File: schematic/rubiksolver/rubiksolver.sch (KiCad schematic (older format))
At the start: 10 parts, among them M1 Stepper_Motor_bipolar, M2 Stepper_Motor_bipolar, M3 Stepper_Motor_bipolar, M4 Stepper_Motor_bipolar

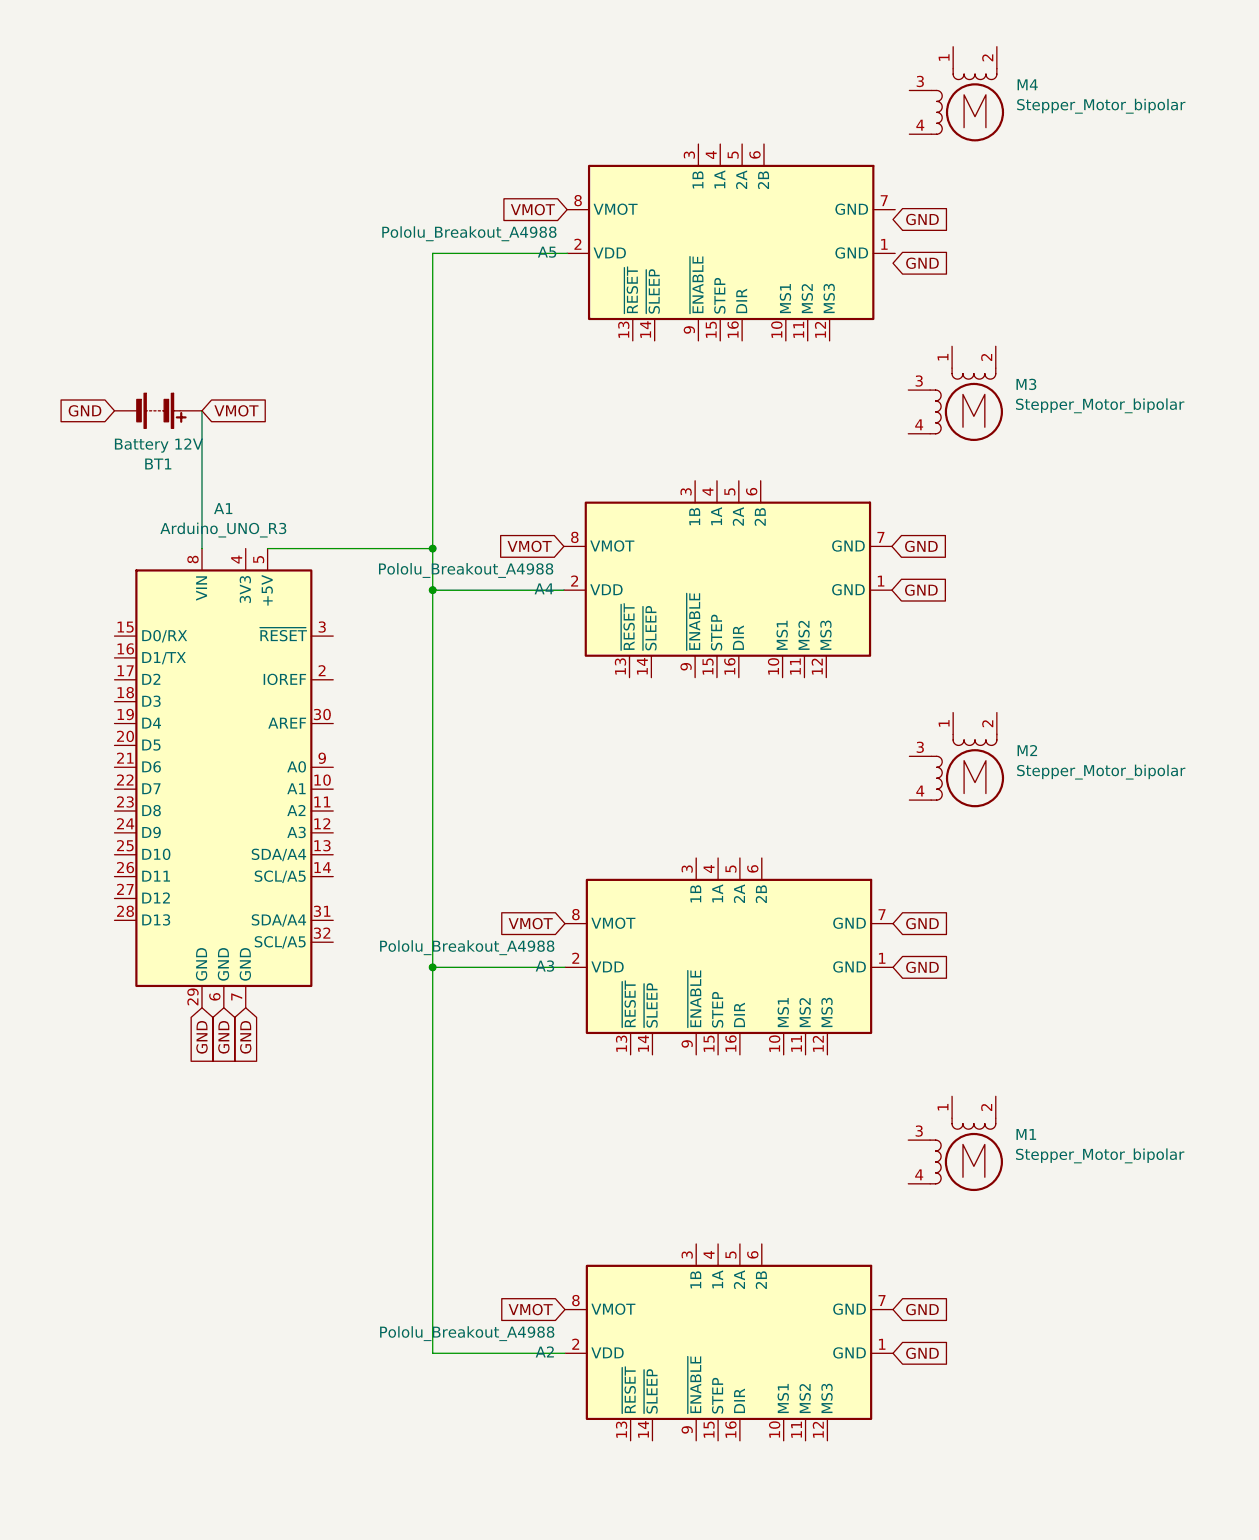
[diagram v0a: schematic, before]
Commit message: Finished schematic
No footprints in yet, need to add
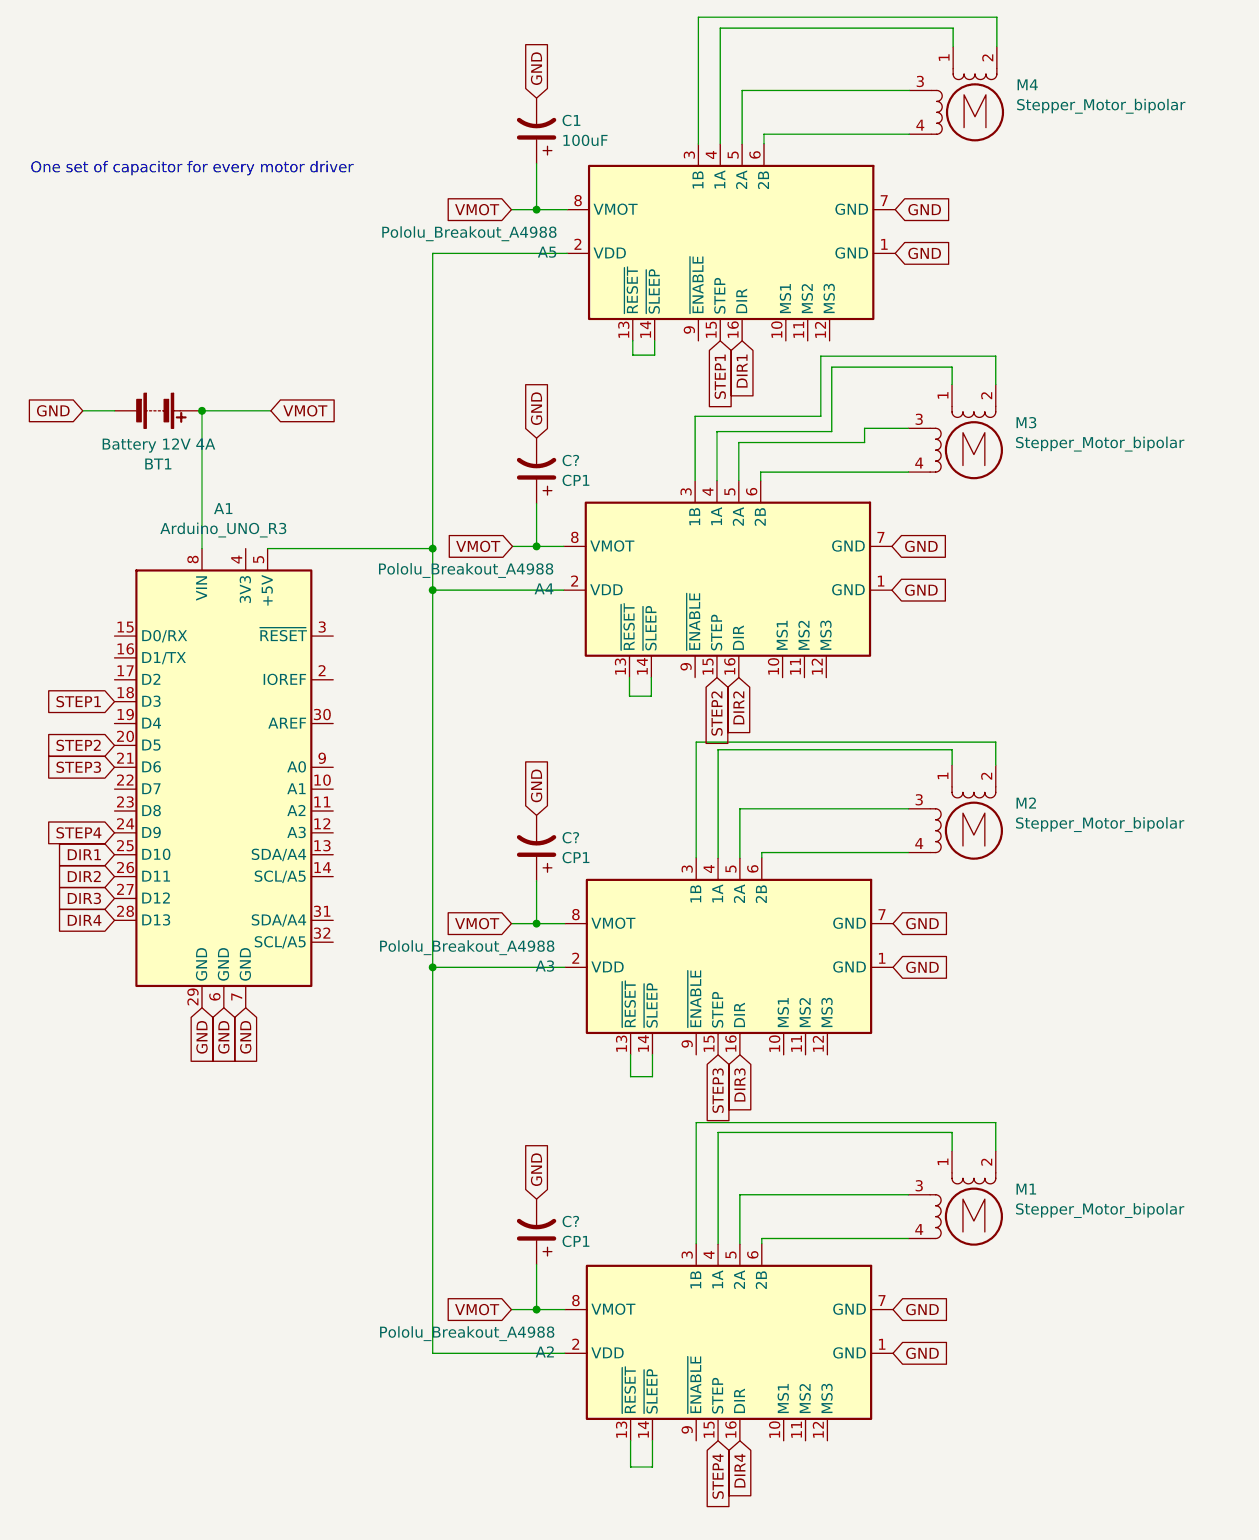
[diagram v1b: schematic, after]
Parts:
- added C1: 100uF, symbol Device:CP1
- added C? (x3): CP1, symbol Device:CP1
- BT1: value Battery 12V -> Battery 12V 4A
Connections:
- net GND: now also A5.1 (GND), A5.7 (GND), C1.2, C?.2, C?.2, C?.2
- net VMOT: now also C1.1, C?.1, C?.1, C?.1
- net at A3.13 (~RESET): now also A3.14 (~SLEEP)
- net STEP3: now reaches A3.15 (STEP)
- net STEP3: now also A1.21 (D6)
- net DIR3: now reaches A3.16 (DIR)
- net DIR3: now also A1.27 (D12)
- net at A3.3 (1B): now also M2.2 (-)
- net at A3.4 (1A): now also M2.1
- net at A3.5 (2A): now also M2.3
- net at A3.6 (2B): now also M2.4
- net at A4.13 (~RESET): now also A4.14 (~SLEEP)
- net STEP2: now reaches A4.15 (STEP)
- net STEP2: now also A1.20 (D5)
- net DIR2: now reaches A4.16 (DIR)
- net DIR2: now also A1.26 (D11)
- net at A4.3 (1B): now also M3.2 (-)
- net at A4.4 (1A): now also M3.1
- net at A4.5 (2A): now also M3.3
- net at A4.6 (2B): now also M3.4
- net at A5.13 (~RESET): now also A5.14 (~SLEEP)
- net STEP1: now reaches A5.15 (STEP)
- net STEP1: now also A1.18 (D3)
- net DIR1: now reaches A5.16 (DIR)
- net DIR1: now also A1.25 (D10)
- net at A5.3 (1B): now also M4.2 (-)
- net at A5.4 (1A): now also M4.1
- net at A5.5 (2A): now also M4.3
- net at A5.6 (2B): now also M4.4
- net at A2.13 (~RESET): now also A2.14 (~SLEEP)
- net STEP4: now reaches A2.15 (STEP)
- net STEP4: now also A1.24 (D9)
- net DIR4: now reaches A2.16 (DIR)
- net DIR4: now also A1.28 (D13)
- net at A2.3 (1B): now also M1.2 (-)
- net at A2.4 (1A): now also M1.1
- net at A2.5 (2A): now also M1.3
- net at A2.6 (2B): now also M1.4
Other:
- note added: "One set of capacitor for every motor driver\n"
- moved on the sheet: M1, M2, M3
